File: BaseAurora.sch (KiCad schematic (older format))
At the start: 43 parts, among them J1 Conn_01x04_Male, J10 Conn_01x03_Male, J11 Screw_Terminal_01x02, J2 Conn_01x05_Male, J3 Screw_Terminal_01x02, J4 Conn_01x04_Male, J5 Conn_01x04_Male, J6 Screw_Terminal_01x02, J7 Screw_Terminal_01x02, J8 Header_1x2, J9 Header_1x2, K1 HK4100F-DC3V-SHG, Q1 2N3906, Q2 PN2222A, U1 ME6217C33M5G, U2 E32-915T20D, U3 4N32M, U4 NodeMCU1.0(ESP-12E)

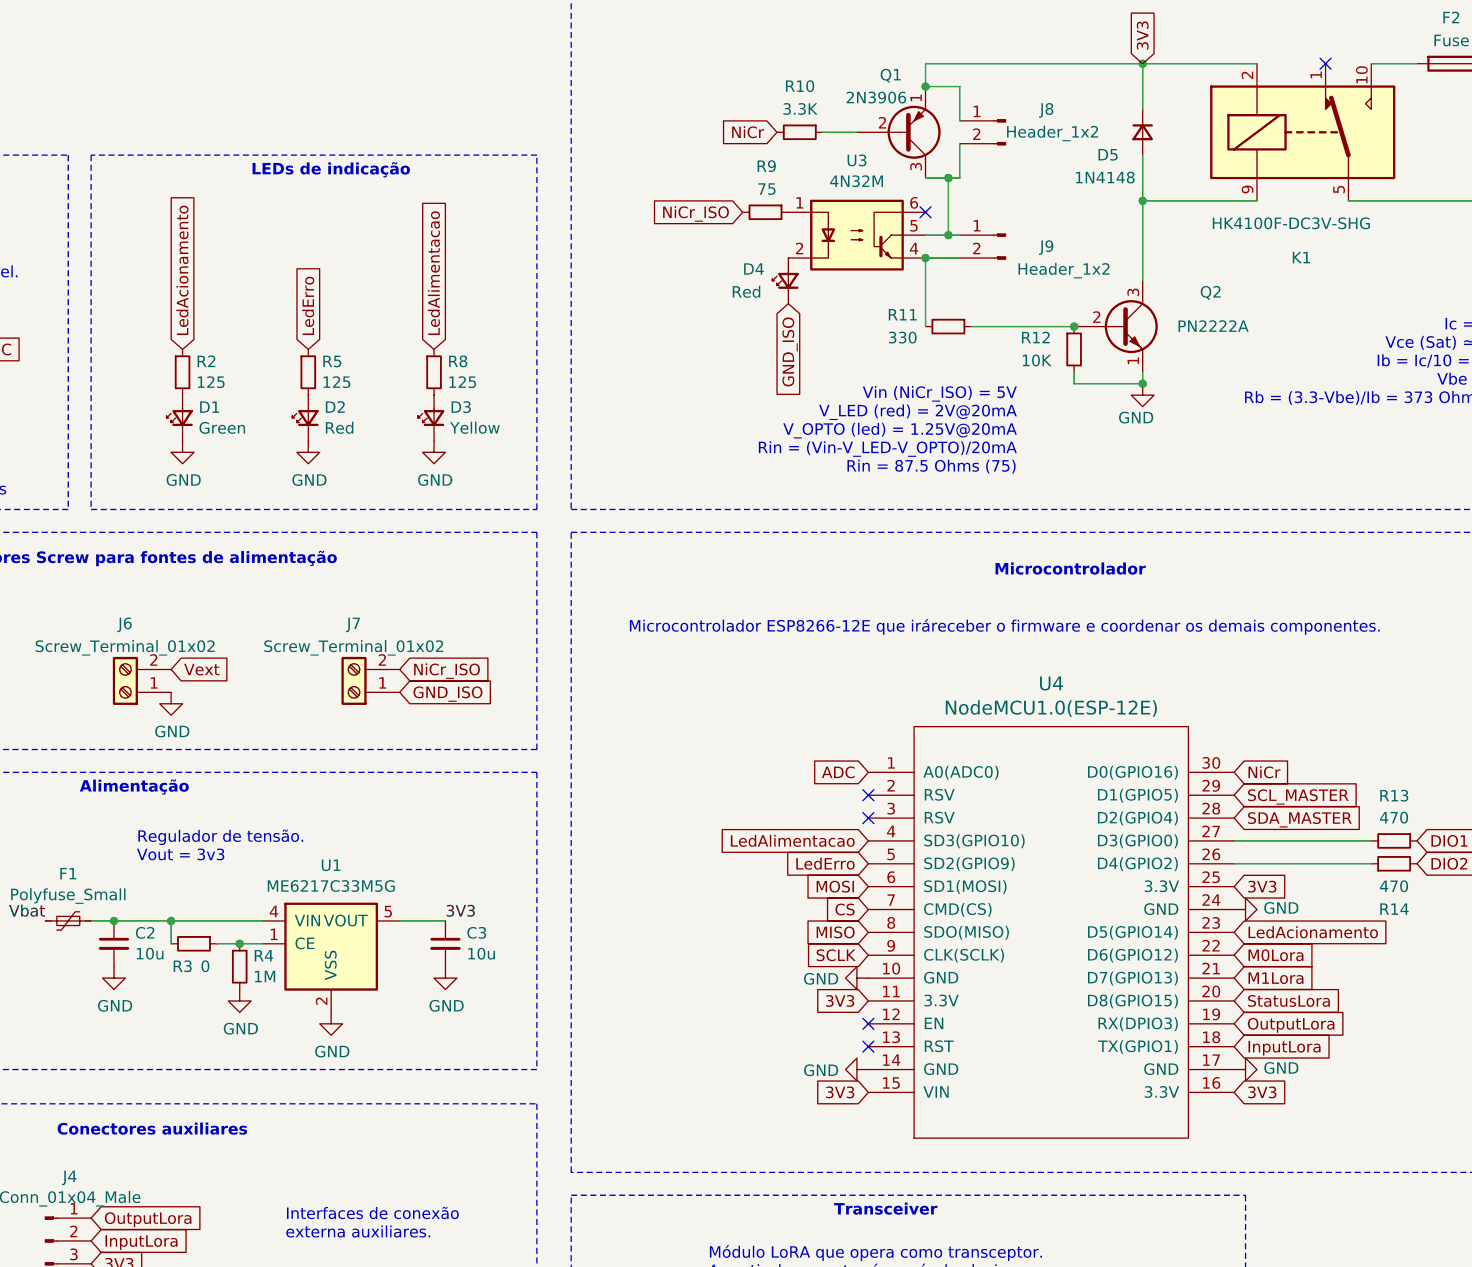
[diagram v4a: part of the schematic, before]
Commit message: Refatoração do component placement e design das tracks seguindo o novo fator de forma. Exclusão de um dos leds e reposicionamento da conexão NiCr.
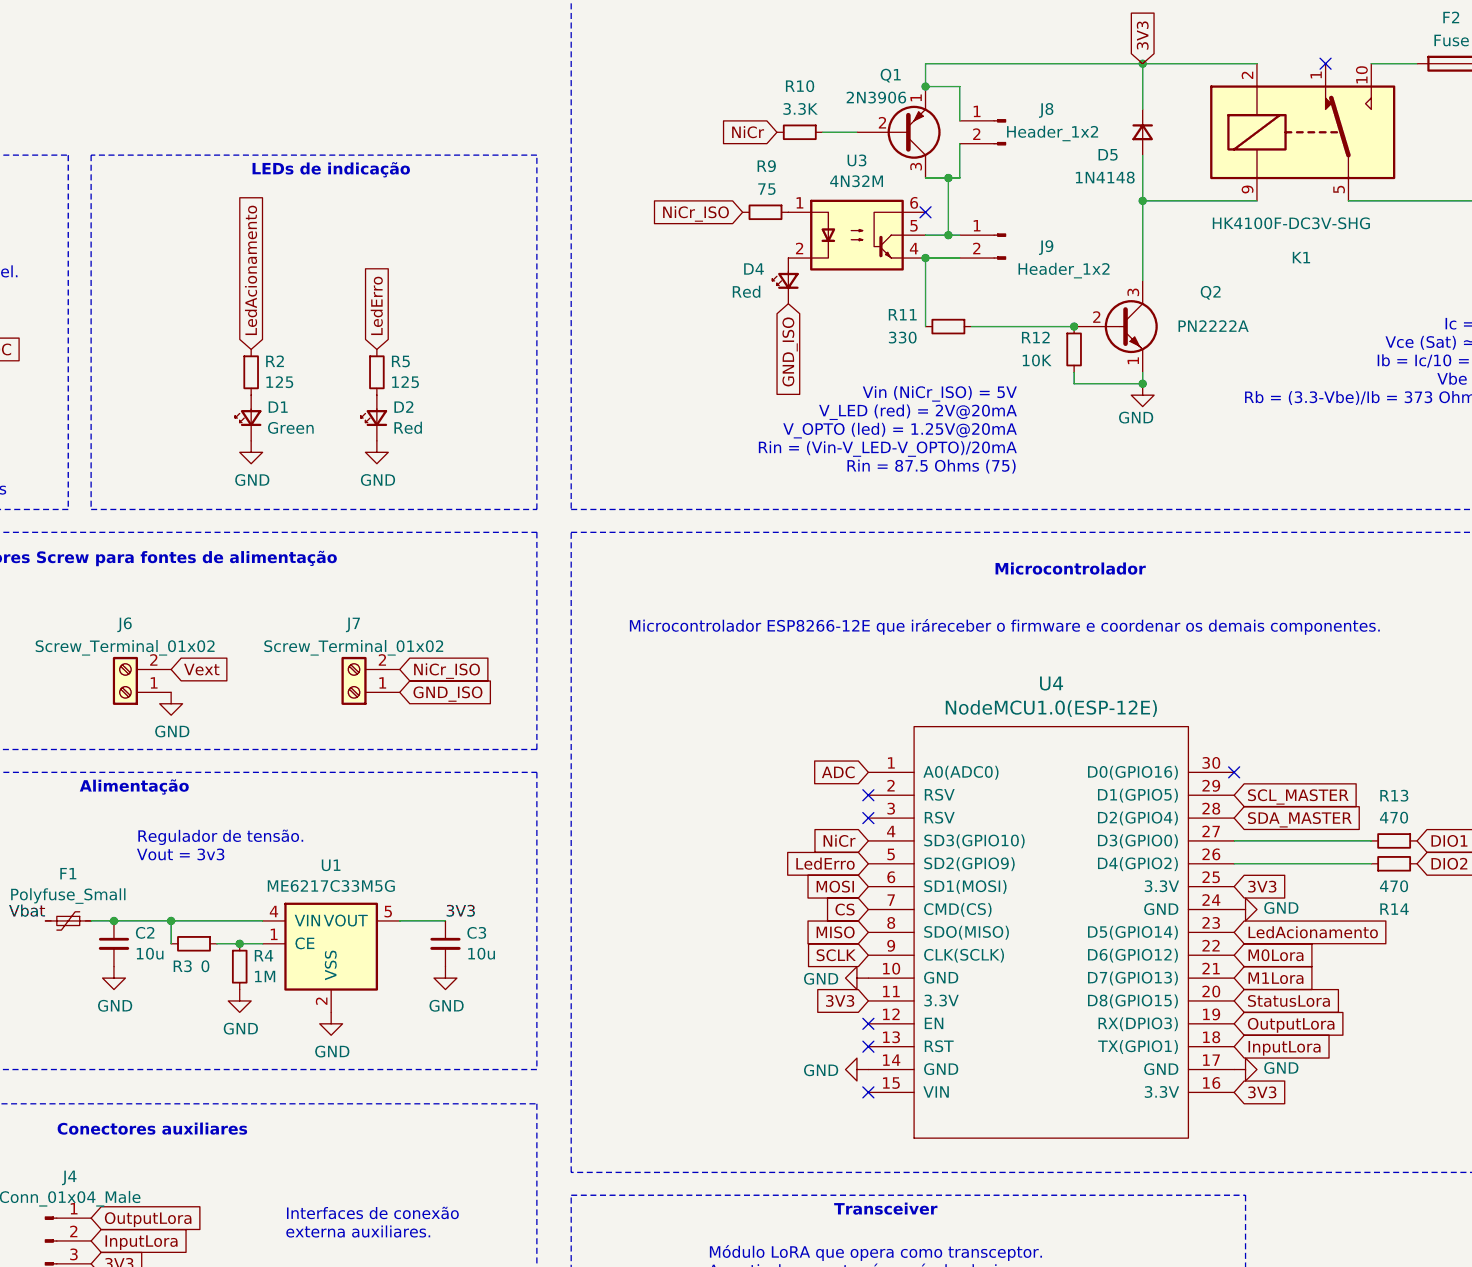
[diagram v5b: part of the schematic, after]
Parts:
- removed D3: Yellow, LED_THT:LED_D3.0mm_Horizontal_O1.27mm_Z2.0mm, symbol Device:LED_Small
- removed R8: 125, Resistor_SMD:R_0805_2012Metric, symbol Device:R_Small
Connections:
- net LedAlimentacao is gone; now on net NiCr: U4.4 (SD3(GPIO10))
- net 3V3: no longer U4.15 (VIN)
- net NiCr: no longer U4.30 (D0(GPIO16))
- no-connect marks 6 -> 8
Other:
- moved on the sheet: D1, D2, R2, R5
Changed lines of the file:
@@
 Wire Wire Line
 	6450 1650 6450 2000
-Text GLabel 5250 4450 0    50   Input ~ 0
-LedAlimentacao
-Text GLabel 3350 2300 1    50   Input ~ 0
-LedAlimentacao
 Text GLabel 5250 4550 0    50   Input ~ 0
 LedErro
-Text GLabel 2800 2300 1    50   Input ~ 0
+Text GLabel 3100 2300 1    50   Input ~ 0
 LedErro
 Text GLabel 6850 4850 2    50   Input ~ 0
@@
 Text GLabel 6850 5050 2    50   Input ~ 0
 M1Lora
-Text GLabel 6850 4150 2    50   Input ~ 0
+Text GLabel 5250 4450 0    50   Input ~ 0
 NiCr
 $Comp
@@
 $EndComp
 $Comp
-L MCU_ESP82:NodeMCU1.0(ESP-12E) U4
-U 1 1 622BF832
-P 6050 4850
-F 0 "U4" H 6050 5937 60  0000 C CNN
-F 1 "NodeMCU1.0(ESP-12E)" H 6050 5831 60  0000 C CNN
-F 2 "ESP8266:ESP12F-Devkit-V3" H 5450 4000 60  0001 C CNN
-F 3 "" H 5450 4000 60  0000 C CNN
-	1    6050 4850
-	1    0    0    -1
-$EndComp
-$Comp
 L Device:R_Small R11
 U 1 1 622C6F91
@@
 Text GLabel 5250 4150 0    50   Input ~ 0
 ADC
-Text GLabel 5250 5550 0    50   Input ~ 0
-3V3
 $Comp
 L Device:LED_Small D1
 U 1 1 62285F2B
-P 2250 2600
-F 0 "D1" V 2296 2530 50  0000 R CNN
-F 1 "Green" V 2205 2530 50  0000 R CNN
-F 2 "LED_THT:LED_D3.0mm_Horizontal_O1.27mm_Z2.0mm" V 2250 2600 50  0001 C CNN
-F 3 "~" V 2250 2600 50  0001 C CNN
-	1    2250 2600
+P 2550 2600
+F 0 "D1" V 2596 2530 50  0000 R CNN
+F 1 "Green" V 2505 2530 50  0000 R CNN
+F 2 "LED_THT:LED_D3.0mm_Horizontal_O1.27mm_Z2.0mm" V 2550 2600 50  0001 C CNN
+F 3 "~" V 2550 2600 50  0001 C CNN
+	1    2550 2600
 	0    -1   -1   0
 $EndComp
@@
 L Device:R_Small R2
 U 1 1 622874A4
-P 2250 2400
-F 0 "R2" H 2309 2446 50  0000 L CNN
-F 1 "125" H 2309 2355 50  0000 L CNN
-F 2 "Resistor_SMD:R_0805_2012Metric" H 2250 2400 50  0001 C CNN
-F 3 "~" H 2250 2400 50  0001 C CNN
-	1    2250 2400
+P 2550 2400
+F 0 "R2" H 2609 2446 50  0000 L CNN
+F 1 "125" H 2609 2355 50  0000 L CNN
+F 2 "Resistor_SMD:R_0805_2012Metric" H 2550 2400 50  0001 C CNN
+F 3 "~" H 2550 2400 50  0001 C CNN
+	1    2550 2400
 	1    0    0    -1
 $EndComp
@@
 L Device:LED_Small D2
 U 1 1 622880AD
-P 2800 2600
-F 0 "D2" V 2846 2530 50  0000 R CNN
-F 1 "Red" V 2755 2530 50  0000 R CNN
-F 2 "LED_THT:LED_D3.0mm_Horizontal_O1.27mm_Z2.0mm" V 2800 2600 50  0001 C CNN
-F 3 "~" V 2800 2600 50  0001 C CNN
-	1    2800 2600
-	0    -1   -1   0
-$EndComp
-$Comp
-L Device:LED_Small D3
-U 1 1 622889DB
-P 3350 2600
-F 0 "D3" V 3396 2530 50  0000 R CNN
-F 1 "Yellow" V 3305 2530 50  0000 R CNN
-F 2 "LED_THT:LED_D3.0mm_Horizontal_O1.27mm_Z2.0mm" V 3350 2600 50  0001 C CNN
-F 3 "~" V 3350 2600 50  0001 C CNN
-	1    3350 2600
+P 3100 2600
+F 0 "D2" V 3146 2530 50  0000 R CNN
+F 1 "Red" V 3055 2530 50  0000 R CNN
+F 2 "LED_THT:LED_D3.0mm_Horizontal_O1.27mm_Z2.0mm" V 3100 2600 50  0001 C CNN
+F 3 "~" V 3100 2600 50  0001 C CNN
+	1    3100 2600
 	0    -1   -1   0
 $EndComp
@@
 L Device:R_Small R5
 U 1 1 622891C0
-P 2800 2400
-F 0 "R5" H 2859 2446 50  0000 L CNN
-F 1 "125" H 2859 2355 50  0000 L CNN
-F 2 "Resistor_SMD:R_0805_2012Metric" H 2800 2400 50  0001 C CNN
-F 3 "~" H 2800 2400 50  0001 C CNN
-	1    2800 2400
-	1    0    0    -1
-$EndComp
-$Comp
-L Device:R_Small R8
-U 1 1 622895C0
-P 3350 2400
-F 0 "R8" H 3409 2446 50  0000 L CNN
-F 1 "125" H 3409 2355 50  0000 L CNN
-F 2 "Resistor_SMD:R_0805_2012Metric" H 3350 2400 50  0001 C CNN
-F 3 "~" H 3350 2400 50  0001 C CNN
-	1    3350 2400
-	1    0    0    -1
-$EndComp
-Text GLabel 2250 2300 1    50   Input ~ 0
+P 3100 2400
+F 0 "R5" H 3159 2446 50  0000 L CNN
+F 1 "125" H 3159 2355 50  0000 L CNN
+F 2 "Resistor_SMD:R_0805_2012Metric" H 3100 2400 50  0001 C CNN
+F 3 "~" H 3100 2400 50  0001 C CNN
+	1    3100 2400
+	1    0    0    -1
+$EndComp
+Text GLabel 2550 2300 1    50   Input ~ 0
 LedAcionamento
 $Comp
@@
 L power:GND #PWR0112
 U 1 1 6229A786
-P 2250 2700
-F 0 "#PWR0112" H 2250 2450 50  0001 C CNN
-F 1 "GND" H 2255 2527 50  0000 C CNN
-F 2 "" H 2250 2700 50  0001 C CNN
-F 3 "" H 2250 2700 50  0001 C CNN
-	1    2250 2700
+P 2550 2700
+F 0 "#PWR0112" H 2550 2450 50  0001 C CNN
+F 1 "GND" H 2555 2527 50  0000 C CNN
+F 2 "" H 2550 2700 50  0001 C CNN
+F 3 "" H 2550 2700 50  0001 C CNN
+	1    2550 2700
 	1    0    0    -1
 $EndComp
@@
 L power:GND #PWR0113
 U 1 1 6229AA84
-P 2800 2700
-F 0 "#PWR0113" H 2800 2450 50  0001 C CNN
-F 1 "GND" H 2805 2527 50  0000 C CNN
-F 2 "" H 2800 2700 50  0001 C CNN
-F 3 "" H 2800 2700 50  0001 C CNN
-	1    2800 2700
-	1    0    0    -1
-$EndComp
-$Comp
-L power:GND #PWR0114
-U 1 1 6229AEDE
-P 3350 2700
-F 0 "#PWR0114" H 3350 2450 50  0001 C CNN
-F 1 "GND" H 3355 2527 50  0000 C CNN
-F 2 "" H 3350 2700 50  0001 C CNN
-F 3 "" H 3350 2700 50  0001 C CNN
-	1    3350 2700
+P 3100 2700
+F 0 "#PWR0113" H 3100 2450 50  0001 C CNN
+F 1 "GND" H 3105 2527 50  0000 C CNN
+F 2 "" H 3100 2700 50  0001 C CNN
+F 3 "" H 3100 2700 50  0001 C CNN
+	1    3100 2700
 	1    0    0    -1
 $EndComp
@@
 Wire Wire Line
 	8000 1050 8000 1250
+NoConn ~ 5250 5550
+$Comp
+L MCU_ESP82:NodeMCU1.0(ESP-12E) U4
+U 1 1 622BF832
+P 6050 4850
+F 0 "U4" H 6050 5937 60  0000 C CNN
+F 1 "NodeMCU1.0(ESP-12E)" H 6050 5831 60  0000 C CNN
+F 2 "ESP8266:ESP12F-Devkit-V3" H 5450 4000 60  0001 C CNN
+F 3 "" H 5450 4000 60  0000 C CNN
+	1    6050 4850
+	1    0    0    -1
+$EndComp
+NoConn ~ 6850 4150
 $EndSCHEMATC
